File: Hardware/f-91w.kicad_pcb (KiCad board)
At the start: 2 copper layers, 24.4 x 24.4 mm, 37 parts, among them P1 CONN_01X01, P10 CONN_01X01, P11 CONN_01X01, P13 CONN_01X01, P14 CONN_01X01, P15 CONN_01X01, P2 CONN_01X01, P3 CONN_01X01, P4 CONN_01X01, P5 CONN_01X01, P6 CONN_01X01, P7 CONN_01X01, P8 CONN_01X01, P9 CONN_01X01, Q1 BC846, U1 MSP430FR6972, U2 LCD-F-91W, U3 TSOP57xxx, U4 MAG3110

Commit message: Add temporary symbols to check
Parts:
- removed MH1, MH2, MH3, MH4, MH5, MH6, MH7: 1pin, Connect:1pin
- removed P1, P2, P3, P4: CONN_01X01, Connect:1pin
- removed U4: MAG3110, f-91w:DFN-10-1EP_2x2mm_Pitch0.4mm
- added C10: 0.1uF, Capacitor_SMD:C_0402_1005Metric, F.Cu at (86.4, 110.4)
- added C11: 0.1uF, Capacitor_SMD:C_0402_1005Metric, F.Cu at (98.7, 98.7)
- added C9: 22pF, Capacitor_SMD:C_0402_1005Metric, F.Cu at (93.8, 105.8)
- added J1: UART, Connector_PinHeader_1.00mm:PinHeader_1x02_P1.00mm_Vertical, F.Cu at (95.6, 102.3)
- added J2: Programming connector, Connector_PinHeader_1.00mm:PinHeader_1x05_P1.00mm_Vertical, F.Cu at (95.6, 95.3)
- added R4: R, Resistor_SMD:R_0402_1005Metric, F.Cu at (80.6, 110.9)
- added Y1: 32.768 kHz, Crystal:Crystal_AT310_D3.0mm_L10.0mm_Horizontal, F.Cu at (80.7, 95.1)
- C1: value 4.7u -> 0.1uf; footprint Capacitors_SMD:C_0402 -> Capacitor_SMD:C_0402_1005Metric
- C2, C3: value 22p -> 0.1uf; footprint Capacitors_SMD:C_0402 -> Capacitor_SMD:C_0402_1005Metric
- C4: value 100n -> C; footprint Capacitors_SMD:C_0402 -> Capacitor_SMD:C_0402_1005Metric
- C5, C6: value 100n -> 0.1uf; footprint Capacitors_SMD:C_0402 -> Capacitor_SMD:C_0402_1005Metric
- C7: value 100n -> 10uf; footprint Capacitors_SMD:C_0402 -> Capacitor_SMD:C_0402_1005Metric
- C8: value 100n -> 22pF; footprint Capacitors_SMD:C_0402 -> Capacitor_SMD:C_0402_1005Metric
- Q1: footprint f-91w:SOT416 -> Package_TO_SOT_SMD:SOT-23
- R1: value 10k -> R; footprint Resistors_SMD:R_0402 -> Resistor_SMD:R_0402_1005Metric
- R3: value 10k -> 100
- U1: value MSP430FR6972 -> PIC24FJ128GL306; footprint Housings_DFN_QFN:QFN-64-1EP_9x9mm_Pitch0.5mm -> Package_DFN_QFN:Microchip_DRQFN-64-1EP_7x7mm_P0.65mm_EP4.1x4.1mm
- U3: value TSOP57xxx -> BME280; footprint f-91w:TSOP57xxx -> Package_LGA:LGA-8_3x5mm_P1.25mm
- moved C4 44.7 mm to (101.6, 94.7), turned to 0 degrees
- moved R1 42.5 mm to (90.9, 103.9), turned to 0 degrees
- moved C2 41.3 mm to (104.5, 94.7), turned to 0 degrees
- moved C1 40.2 mm to (98.7, 100.7), turned to 0 degrees
- moved U3 37.4 mm to (87.1, 106.2), turned to 0 degrees
- moved C3 34.8 mm to (98.7, 94.7), turned to 0 degrees
- moved C6 32.4 mm to (101.6, 96.7), turned to 0 degrees
- moved U1 31.4 mm to (89.4, 98.3), turned to 0 degrees
- moved C7 29.5 mm to (98.7, 96.7), turned to 0 degrees
- moved C5 26.6 mm to (90.9, 105.9)
- moved C8 21.1 mm to (83.5, 110.9)
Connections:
- C2 pad 1: /Q-1 -> VCC
- C3 pad 1: /Q-2 -> VCC
- C5 pad 1: GND -> VCC
- C5 pad 2: /MAG_PWR -> GND
- C6 pad 1: Net-(C6-Pad1) -> VCC
- C7 pad 1: Net-(C7-Pad1) -> /VCAP
- C8 pad 1: /MAG_PWR -> GND
- C8 pad 2: GND -> /SOSCO
- P11 pad 1: /LED_1 -> GND
- P15 pad 1: Net-(P15-Pad1) -> unconnected-(P15-Pad1)
- R1 pad 1: VCC -> Net-(P1-Pad1)
- R1 pad 2: Net-(P4-Pad1) -> VCC
- R2 pad 1: Net-(R2-Pad1) -> /BUZ
- U3 pad 1: /IR -> GND
- U3 pad 5: /IR_PWR -> /SDO
- U3 pad 6: GND -> VCC
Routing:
- net (no net): track 0.00 -> 142.1 mm, vias 0 -> 13
- net Net-(P4-Pad1): track 24.2 -> 0.00 mm, vias 2 -> 0
- net Net-(P3-Pad1): track 22.5 -> 0.00 mm
- net GND: track 96.2 -> 117.2 mm, vias 9 -> 13
- net /LED_1: track 19.9 -> 0.00 mm, vias 4 -> 0
- net /SDA: track 16.7 -> 0.00 mm, vias 2 -> 0
- net /MAG_PWR: track 15.7 -> 0.00 mm, vias 3 -> 0
- net /SCL: track 13.7 -> 0.00 mm, vias 2 -> 0
- net /IR_PWR: track 11.2 -> 0.00 mm, vias 2 -> 0
- net /Q-2: track 10.5 -> 0.00 mm
- net unconnected-(P15-Pad1): track 0.00 -> 9.71 mm, vias 0 -> 2
- net Net-(P15-Pad1): track 9.71 -> 0.00 mm, vias 2 -> 0
- net /INT1: track 9.69 -> 0.00 mm, vias 2 -> 0
- net VCC: track 59.1 -> 68.1 mm, vias 6 -> 7
- net /BUZ: track 8.95 -> 0.00 mm, vias 1 -> 0
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
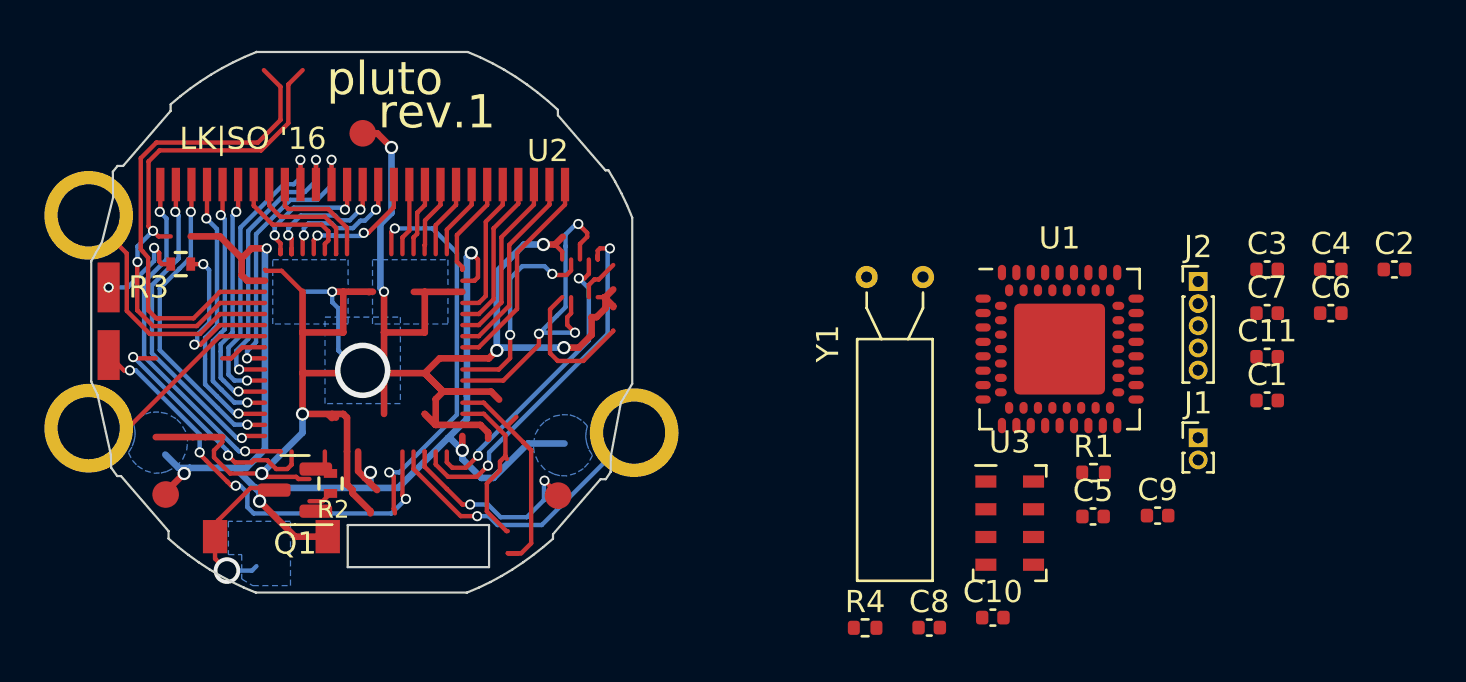
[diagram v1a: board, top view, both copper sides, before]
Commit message: Add BME280 footprint
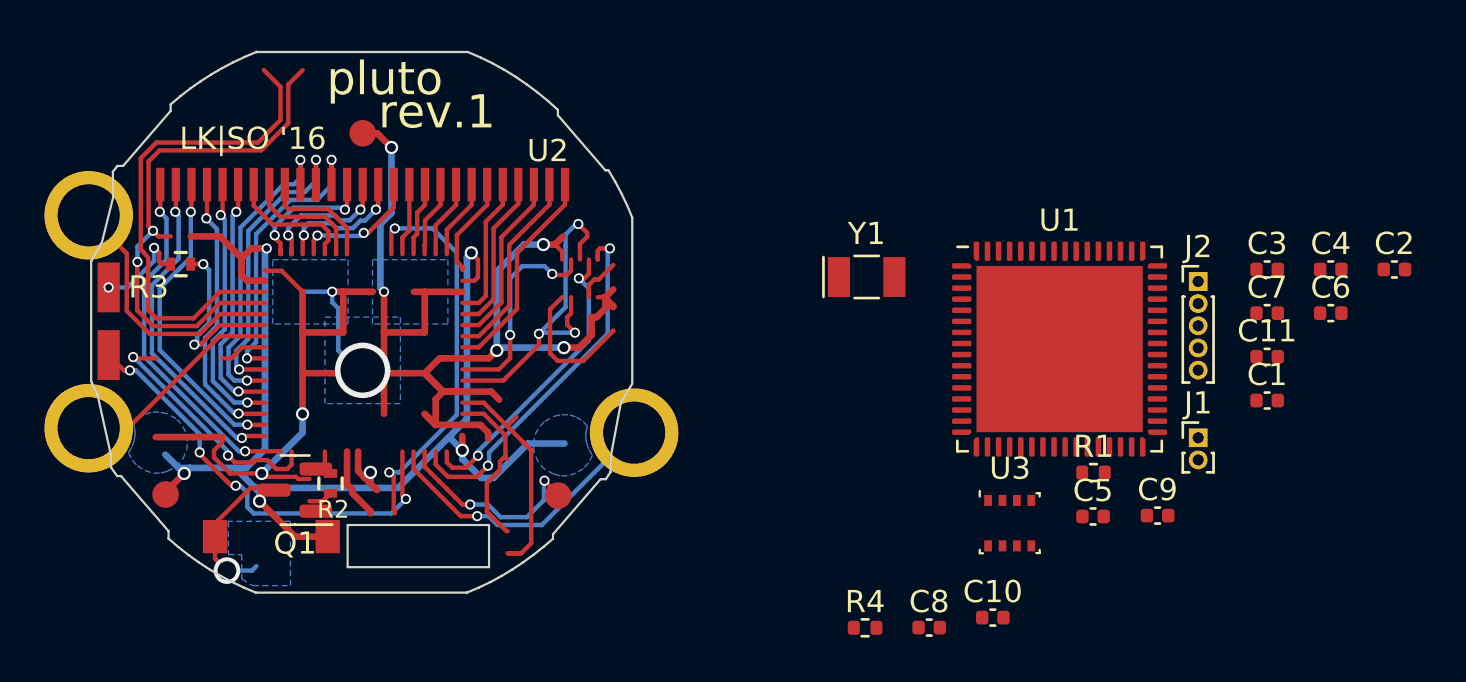
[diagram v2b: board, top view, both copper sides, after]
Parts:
- R1: value R -> 10K
- R4: value R -> 200
- U1: footprint Package_DFN_QFN:Microchip_DRQFN-64-1EP_7x7mm_P0.65mm_EP4.1x4.1mm -> Package_DFN_QFN:QFN-64-1EP_9x9mm_P0.5mm_EP7.5x7.5mm
- U3: footprint Package_LGA:LGA-8_3x5mm_P1.25mm -> Package_LGA:Bosch_LGA-8_2.5x2.5mm_P0.65mm_ClockwisePinNumbering
- Y1: footprint Crystal:Crystal_AT310_D3.0mm_L10.0mm_Horizontal -> Crystal:Crystal_SMD_EuroQuartz_EQ161-2Pin_3.2x1.5mm
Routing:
- net VCC: track 68.1 -> 0.00 mm, vias 7 -> 0
- net /BUZ: track 0.00 -> 68.1 mm, vias 0 -> 7
- net GND: track 117.2 -> 113.1 mm
